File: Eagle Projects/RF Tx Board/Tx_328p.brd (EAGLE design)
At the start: 100 x 80 mm, 12 parts, among them U1 ATMEGA328P_TQFP

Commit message: GPS Code tweaks (tired to think :P)
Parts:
- removed SPI_HEADER: (no value), pinhead:2X03
- added ISP1: AVRISP-BOX, adafruit:AVRISP-BOX
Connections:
- removed net N$4: SPI_HEADER.1
- removed net N$5: SPI_HEADER.3
- removed net N$6: SPI_HEADER.5
- new net RST: ISP1.5
- net GND: now also ISP1.6; no longer SPI_HEADER.6
- net MISO: now also ISP1.1
- net MOSI: now also ISP1.4; no longer SPI_HEADER.4
- net SCK: now also ISP1.3
- net VCC: now also ISP1.2; no longer SPI_HEADER.2
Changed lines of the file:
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@@
 </autorouter>
 <elements>
-<element name="SPI_HEADER" library="pinhead" package="2X03" value="" x="83.82" y="38.1" rot="R90"/>
 <element name="USART" library="pinhead" package="1X02" value="" x="39.37" y="58.42" rot="R270"/>
 <element name="GPS" library="pinhead" package="1X04" value="" x="6.35" y="-3.81"/>
@@
 <element name="C2" library="resistor" package="C0805K" value="0.1uF" x="-7.62" y="-54.61"/>
 <element name="C5" library="resistor" package="C0805K" value="0.1uF" x="-7.62" y="-59.69"/>
+<element name="ISP1" library="adafruit" package="AVRISP-BOX" value="AVRISP-BOX" x="-15.24" y="-53.34"/>
 </elements>
 <signals>
@@
 <contactref element="C2" pad="2"/>
 <contactref element="C5" pad="2"/>
-<contactref element="SPI_HEADER" pad="6"/>
-<wire x1="12.7" y1="-16.51" x2="82.55" y2="40.64" width="0" layer="19" extent="1-1"/>
+<contactref element="ISP1" pad="6"/>
+<wire x1="-6.62" y1="-54.61" x2="-13.843" y2="-55.88" width="0" layer="19" extent="1-1"/>
+<wire x1="-6.62" y1="-59.69" x2="-6.62" y2="-54.61" width="0" layer="19" extent="1-1"/>
+<wire x1="-6.62" y1="-49.53" x2="-6.62" y2="-54.61" width="0" layer="19" extent="1-1"/>
+<wire x1="-6.62" y1="-44.45" x2="-6.62" y2="-49.53" width="0" layer="19" extent="1-1"/>
+<wire x1="12.7" y1="-16.51" x2="-6.62" y2="-44.45" width="0" layer="19" extent="1-1"/>
 <wire x1="2.54" y1="-3.81" x2="12.7" y2="-16.51" width="0" layer="19" extent="1-1"/>
-<wire x1="-6.62" y1="-44.45" x2="12.7" y2="-16.51" width="0" layer="19" extent="1-1"/>
-<wire x1="-6.62" y1="-49.53" x2="-6.62" y2="-44.45" width="0" layer="19" extent="1-1"/>
-<wire x1="-6.62" y1="-54.61" x2="-6.62" y2="-49.53" width="0" layer="19" extent="1-1"/>
-<wire x1="-6.62" y1="-59.69" x2="-6.62" y2="-54.61" width="0" layer="19" extent="1-1"/>
 </signal>
 <signal name="N$3">
@@
 <contactref element="C2" pad="1"/>
 <contactref element="C5" pad="1"/>
-<contactref element="SPI_HEADER" pad="2"/>
-<wire x1="10.16" y1="-3.81" x2="82.55" y2="35.56" width="0" layer="19" extent="1-1"/>
-<wire x1="2.54" y1="-16.51" x2="10.16" y2="-3.81" width="0" layer="19" extent="1-1"/>
-<wire x1="-0.7874" y1="-30.88" x2="2.54" y2="-16.51" width="0" layer="19" extent="1-1"/>
+<contactref element="ISP1" pad="2"/>
+<wire x1="-8.62" y1="-54.61" x2="-8.62" y2="-59.69" width="0" layer="19" extent="1-1"/>
+<wire x1="-8.62" y1="-49.53" x2="-8.62" y2="-54.61" width="0" layer="19" extent="1-1"/>
+<wire x1="-13.843" y1="-50.8" x2="-8.62" y2="-49.53" width="0" layer="19" extent="1-1"/>
+<wire x1="-8.57" y1="-40.64" x2="-8.62" y2="-49.53" width="0" layer="19" extent="1-1"/>
+<wire x1="-9.3726" y1="-30.08" x2="-8.57" y2="-40.64" width="0" layer="19" extent="1-1"/>
+<wire x1="-0.7874" y1="-30.88" x2="-9.3726" y2="-30.08" width="0" layer="19" extent="1-1"/>
 <wire x1="-0.7874" y1="-32.48" x2="-0.7874" y2="-30.88" width="0" layer="19" extent="1-1"/>
-<wire x1="-9.3726" y1="-30.08" x2="-0.7874" y2="-30.88" width="0" layer="19" extent="1-1"/>
-<wire x1="-8.57" y1="-40.64" x2="-9.3726" y2="-30.08" width="0" layer="19" extent="1-1"/>
-<wire x1="-8.62" y1="-49.53" x2="-8.57" y2="-40.64" width="0" layer="19" extent="1-1"/>
-<wire x1="-8.62" y1="-54.61" x2="-8.62" y2="-49.53" width="0" layer="19" extent="1-1"/>
-<wire x1="-8.62" y1="-59.69" x2="-8.62" y2="-54.61" width="0" layer="19" extent="1-1"/>
+<wire x1="2.54" y1="-16.51" x2="-0.7874" y2="-30.88" width="0" layer="19" extent="1-1"/>
+<wire x1="10.16" y1="-3.81" x2="2.54" y2="-16.51" width="0" layer="19" extent="1-1"/>
 </signal>
 <signal name="N$9">
@@
 <signal name="MOSI">
 <contactref element="U1" pad="15"/>
-<contactref element="SPI_HEADER" pad="4"/>
-<wire x1="-3.08" y1="-34.7726" x2="82.55" y2="38.1" width="0" layer="19" extent="1-1"/>
+<contactref element="ISP1" pad="4"/>
+<wire x1="-3.08" y1="-34.7726" x2="-14.097" y2="-53.34" width="0" layer="19" extent="1-1"/>
 </signal>
 <signal name="MISO">
 <contactref element="U1" pad="16"/>
+<contactref element="ISP1" pad="1"/>
+<wire x1="-2.28" y1="-34.7726" x2="-16.637" y2="-50.8" width="0" layer="19" extent="1-1"/>
 </signal>
 <signal name="SCK">
 <contactref element="U1" pad="17"/>
+<contactref element="ISP1" pad="3"/>
+<wire x1="-0.7874" y1="-33.28" x2="-16.383" y2="-53.34" width="0" layer="19" extent="1-1"/>
 </signal>
-<signal name="N$4">
-<contactref element="SPI_HEADER" pad="1"/>
-</signal>
-<signal name="N$5">
-<contactref element="SPI_HEADER" pad="3"/>
-</signal>
-<signal name="N$6">
-<contactref element="SPI_HEADER" pad="5"/>
+<signal name="RST">
+<contactref element="ISP1" pad="5"/>
 </signal>
 </signals>

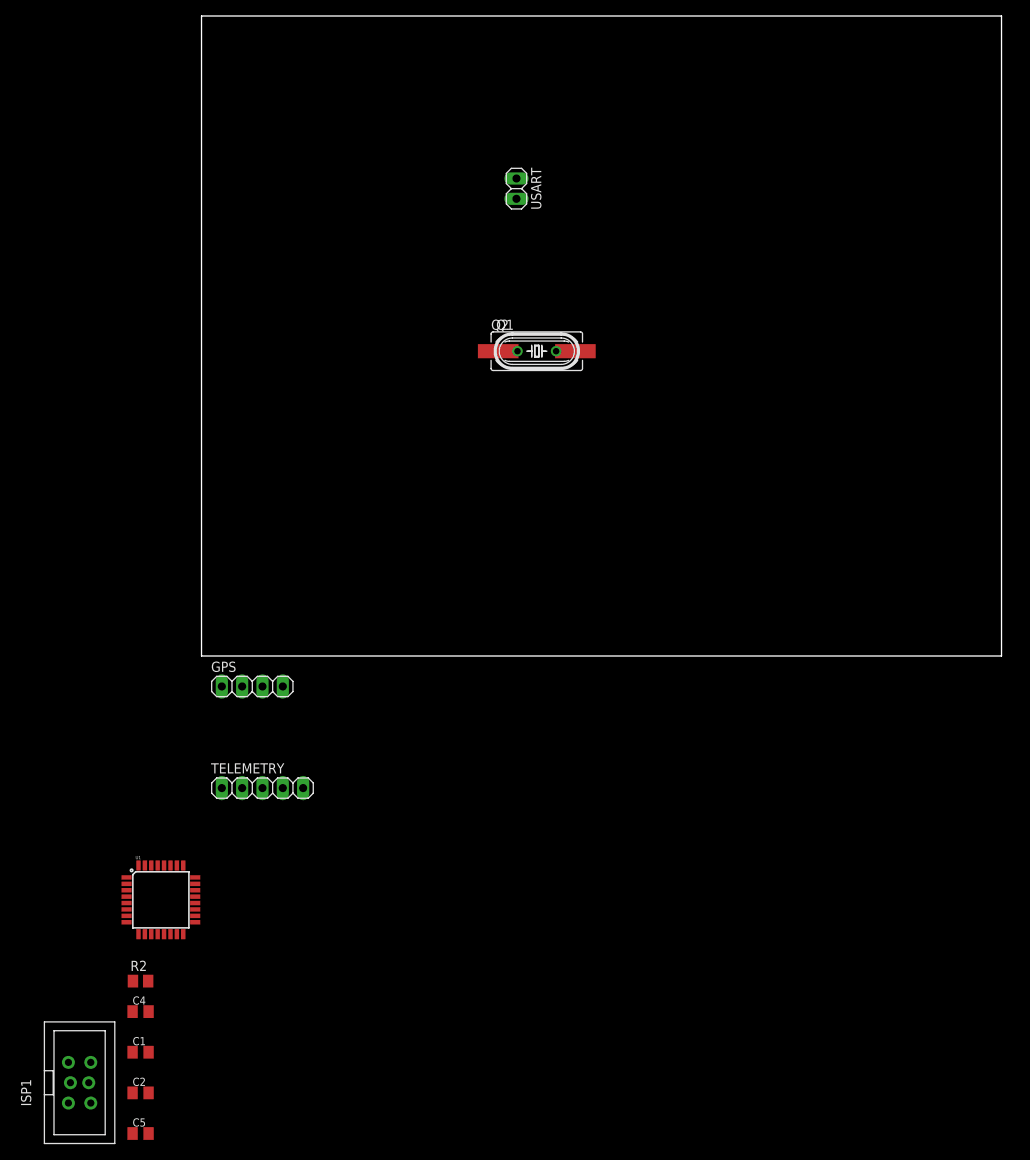
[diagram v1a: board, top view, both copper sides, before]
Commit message: Added Tx/Rx LEDs for board + measurements of GPS & RF boards for comparison *cough*Autorouted *cough* and still broken, redoing manually :P
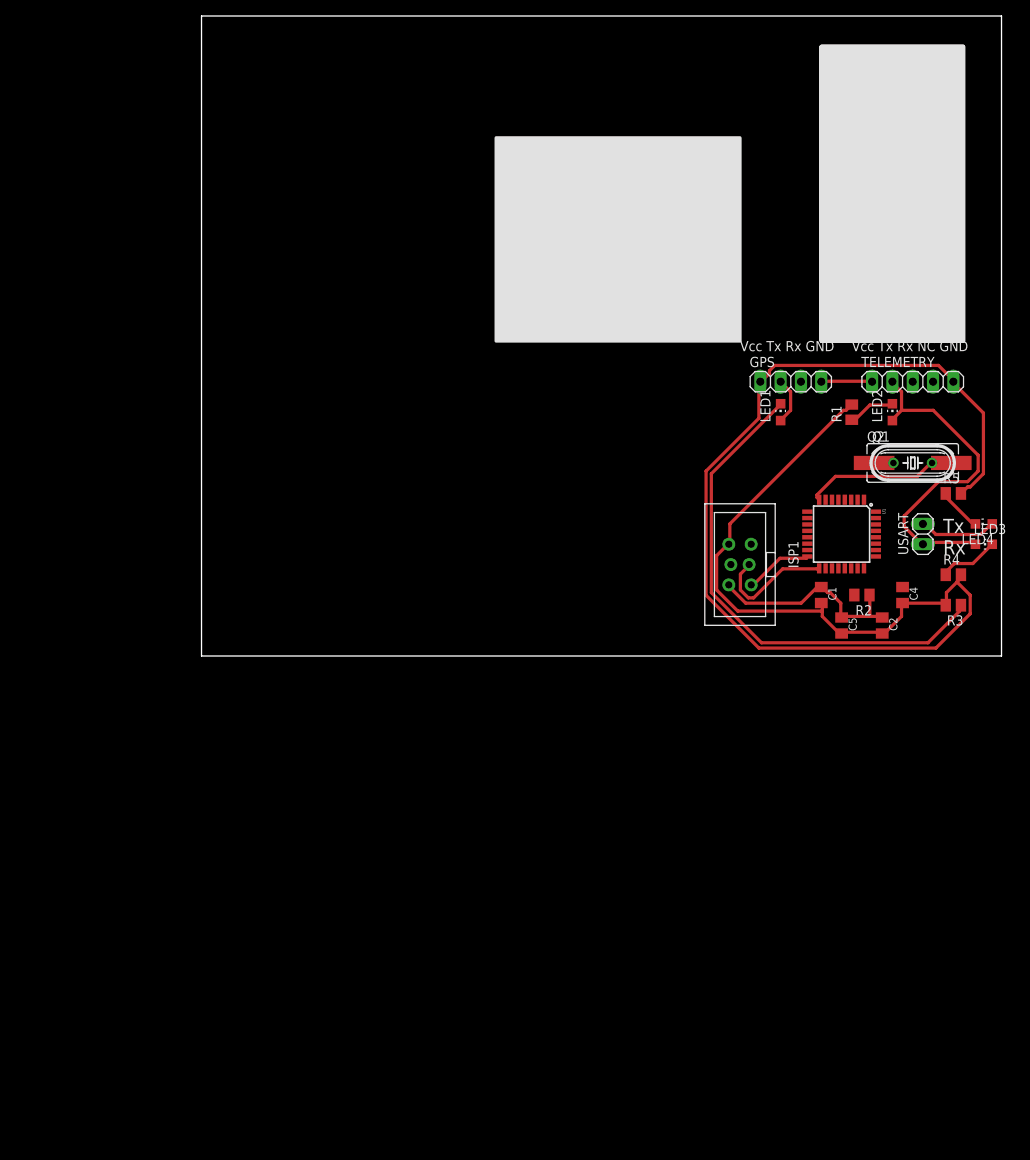
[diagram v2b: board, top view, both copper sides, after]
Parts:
- added LED1, LED2, LED3, LED4: (no value), led:CHIP-LED0805
- added R1, R3, R4, R5: 1k, rcl:M0805
- moved C2 109.6 mm to (85.1, 3.81), turned to 270 degrees
- moved C4 108.6 mm to (87.6, 7.62), turned to 270 degrees
- moved C5 108.2 mm to (80.0, 3.81), turned to 270 degrees
- moved ISP1 104.9 mm to (67.3, 11.4), turned to 180 degrees
- moved C1 102.5 mm to (77.5, 7.62), turned to 270 degrees
- moved R2 102.3 mm to (82.5, 7.62), turned to 180 degrees
- moved U1 96.6 mm to (80.0, 15.2), turned to 270 degrees
- moved TELEMETRY 95.8 mm to (88.9, 34.3)
- moved GPS 77.3 mm to (73.7, 34.3)
- moved USART 66.7 mm to (90.2, 15.2), turned to 90 degrees
- moved Q1 49.0 mm to (88.9, 24.1)
- moved Q2 49.0 mm to (88.9, 24.1)
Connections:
- new net N$4: LED1.C, R3.1
- new net N$5: LED2.C, R1.1
- new net N$6: LED3.C, R4.1
- new net N$8: LED4.C, R5.1
- net GND: now also R1.2, R3.2, R4.2, R5.2
- net RX0: now also LED1.A, LED4.A
- net TX0: now also LED2.A, LED3.A
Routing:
- net GND: track 0.00 -> 185.3 mm
- net N$4: track 0.00 -> 63.3 mm
- net TX0: track 0.00 -> 42.6 mm
- net VCC: track 0.00 -> 33.0 mm
- net N$2: track 0.00 -> 19.2 mm
- net RX0: track 0.00 -> 15.6 mm
- net SCK: track 0.00 -> 15.4 mm
- net MISO: track 0.00 -> 8.52 mm
- net N$6: track 0.00 -> 7.85 mm
- net N$5: track 0.00 -> 6.00 mm
- net N$8: track 0.00 -> 5.76 mm
- net N$1: track 0.00 -> 2.42 mm
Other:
- board text added: "Tx Rx"
- board text added: "Vcc Tx Rx GND"
- board text added: "Vcc Tx Rx NC GND"

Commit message: Misc board tweaks
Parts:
- added ..2: 1k, rcl:M0805
- added PWR_LED: (no value), led:CHIP-LED0805
- added RESET: TAC_SWITCHSMD, SparkFun-Retired:TACTILE-SWITCH-SMD
- added S1: SKHMPSE010, switch:SKHMPXE010
- C1, C2, C4, C5: device resistor:C0805K -> resistor:C0805
- renumbered LED1 to TX_LED_GPS, LED2 to RX_3DR_LED, LED3 to RX_LED, LED4 to TX_LED, R4 to .., R5 to .
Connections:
- new net N$7: ..2.1, PWR_LED.A
- net GND: now also PWR_LED.C, RESET.1, RESET.2, S1.1, S1.2
- net VCC: now also ..2.2, RESET.3, RESET.4, S1.3, S1.4
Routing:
- net GND: track 185.3 -> 213.9 mm
- net VCC: track 33.0 -> 50.0 mm
- net N$7: track 0.00 -> 5.91 mm

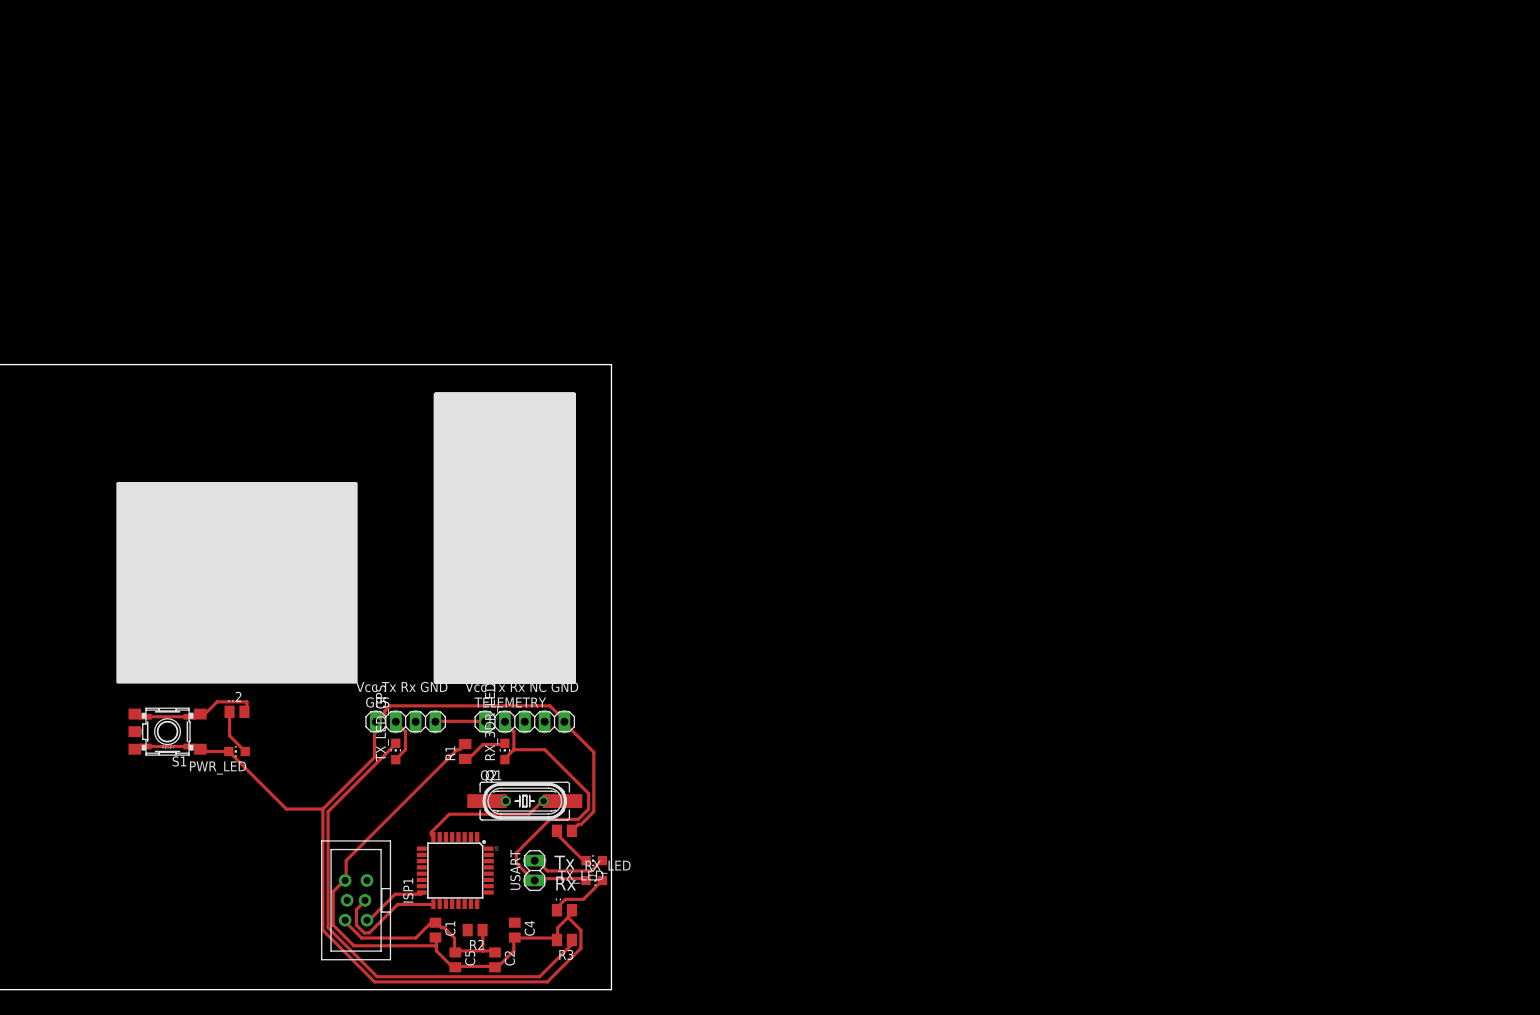
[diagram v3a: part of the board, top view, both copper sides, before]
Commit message: More Board Edits *Imported Ben's CAN PCB layout *Revised schematic for neatness *Added pinheaders as spec'd for SMPS module
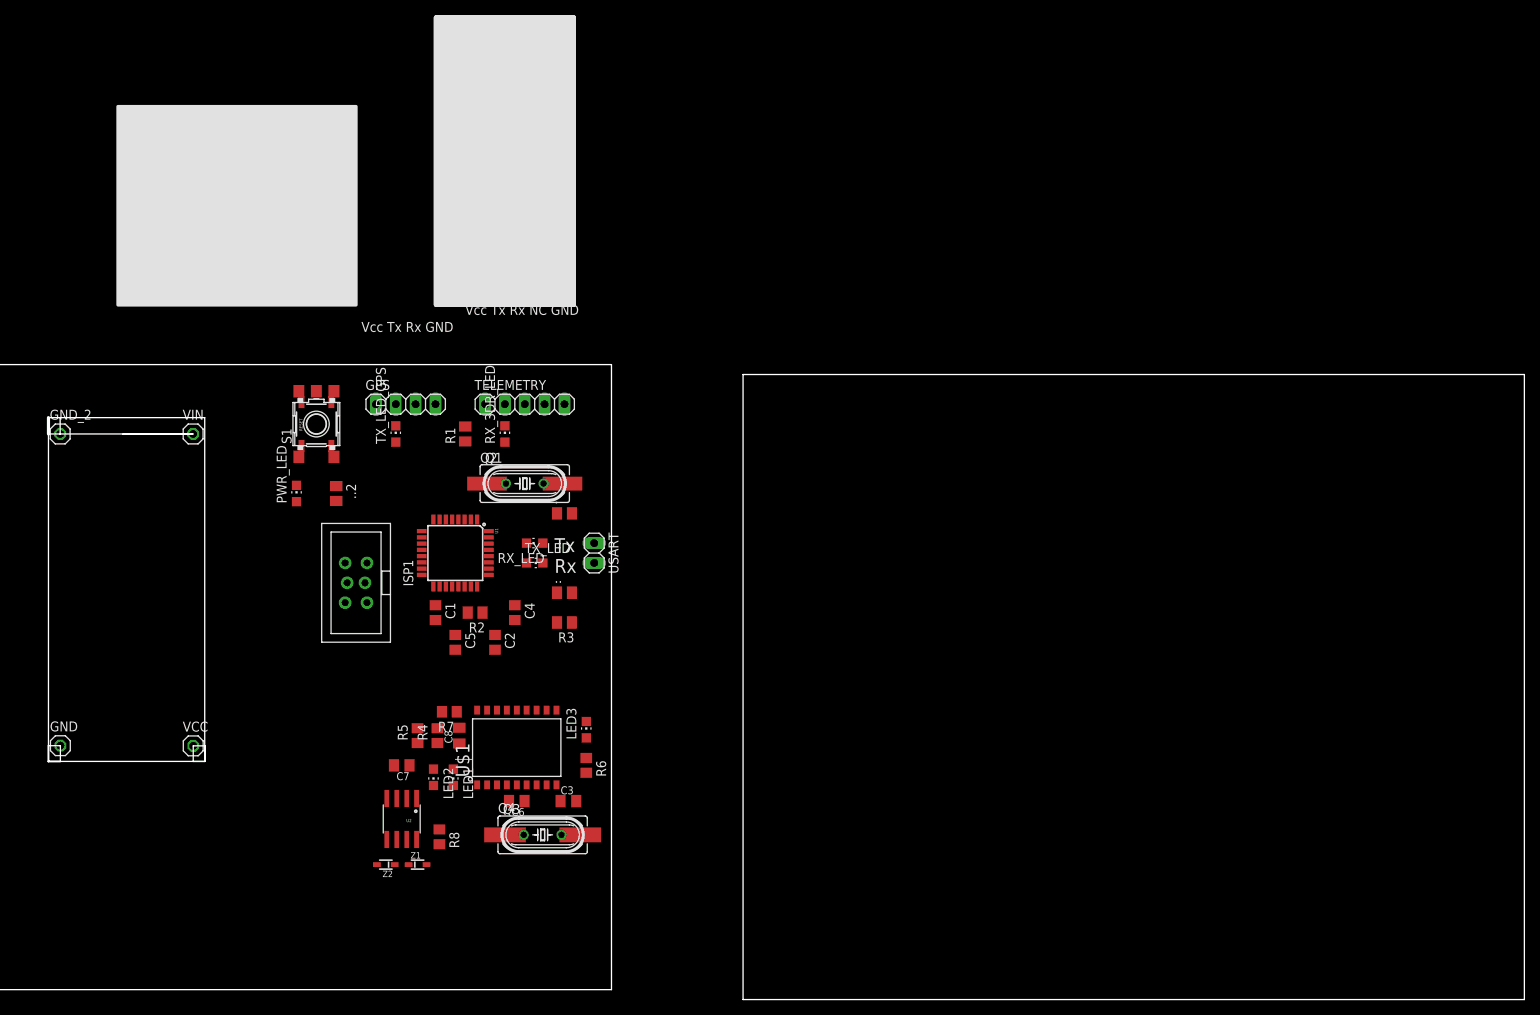
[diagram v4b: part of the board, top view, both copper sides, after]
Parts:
- added C3, C6: 22pF, resistor:C0805K
- added C7, C8: 100nF, resistor:C0805K
- added GND, GND_2, VCC, VIN: (no value), pinhead:1X01
- added LED1: RX, led:CHIP-LED0805
- added LED2: TX, led:CHIP-LED0805
- added LED3: INT, led:CHIP-LED0805
- added Q3: 16MHz, crystal:HC49/S
- added Q4: 16MHz, crystal:HC49UP
- added R4, R5, R6: 1k, resistor:R0805
- added R7, R8: 100k, resistor:R0805
- added U$1: MCP2515SO, RobThePyro:SO-18W
- added U2: MCP2551, SparkFun:SO08
- added Z1, Z2: TVS-UD-SOD323, supressor:SOD323
- moved RX_LED 43.8 mm to (90.2, 57.1), turned to 90 degrees
- moved RESET 43.7 mm to (62.2, 72.4), turned to 90 degrees
- moved S1 43.7 mm to (62.2, 72.4), turned to 90 degrees
- moved USART 41.3 mm to (97.8, 55.9), turned to 270 degrees
- moved GPS 40.6 mm to (73.7, 74.9)
- moved TELEMETRY 40.6 mm to (88.9, 74.9)
- moved . 40.6 mm to (94.0, 61.0)
- moved .. 40.6 mm to (94.0, 50.8)
- moved C1 40.6 mm to (77.5, 48.3)
- moved C2 40.6 mm to (85.1, 44.5)
- moved C4 40.6 mm to (87.6, 48.3)
- moved C5 40.6 mm to (80.0, 44.5)
- moved ISP1 40.6 mm to (67.3, 52.1)
- moved Q1 40.6 mm to (88.9, 64.8)
- moved Q2 40.6 mm to (88.9, 64.8)
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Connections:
- new net +5V: C7.2, C8.2, R4.2, R5.2, R6.2, R7.1, U$1.18, U2.3
- new net CANCS: U$1.16
- new net CANH: U2.7, Z1.C
- new net CANINT: LED3.C, U$1.12
- new net CANL: U2.6, Z2.C
- new net CANRST: R7.2, U$1.17
- new net CANSTBY: R8.1, U2.8
- new net N$10: LED1.A, R4.1
- new net N$11: LED2.A, R5.1
- new net N$12: LED3.A, R6.1
- new net N$13: C3.1, Q3.2, Q4.2, U$1.8
- new net N$14: C6.1, Q3.1, Q4.1, U$1.7
- new net RXCAN: LED1.C, U$1.2, U2.4
- new net TXCAN: LED2.C, U$1.1, U2.1
- net GND: now also C3.2, C6.2, C7.1, C8.1, GND.1, GND_2.1, R8.2, U$1.9, U2.2, Z1.A, Z2.A
- net MISO: now also U$1.15
- net MOSI: now also U$1.14
- net SCK: now also U$1.13
- net VCC: now also VCC.1
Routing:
- net GND: track 213.9 -> 0.00 mm
- net N$4: track 63.3 -> 0.00 mm
- net VCC: track 50.0 -> 0.00 mm
- net TX0: track 42.6 -> 0.00 mm
- net N$2: track 19.2 -> 0.00 mm
- net RX0: track 15.6 -> 0.00 mm
- net SCK: track 15.4 -> 0.00 mm
- net MISO: track 8.52 -> 0.00 mm
- net N$6: track 7.85 -> 0.00 mm
- net N$5: track 6.00 -> 0.00 mm
- net N$7: track 5.91 -> 0.00 mm
- net N$8: track 5.76 -> 0.00 mm
- net N$1: track 2.42 -> 0.00 mm
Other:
- board size 100 x 80 mm -> 216.8 x 81.3 mm
